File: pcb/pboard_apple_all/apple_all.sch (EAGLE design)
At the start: 33 parts, among them IC1 STM32F072C8T6, SW1 324_SW, SW2 324_SW

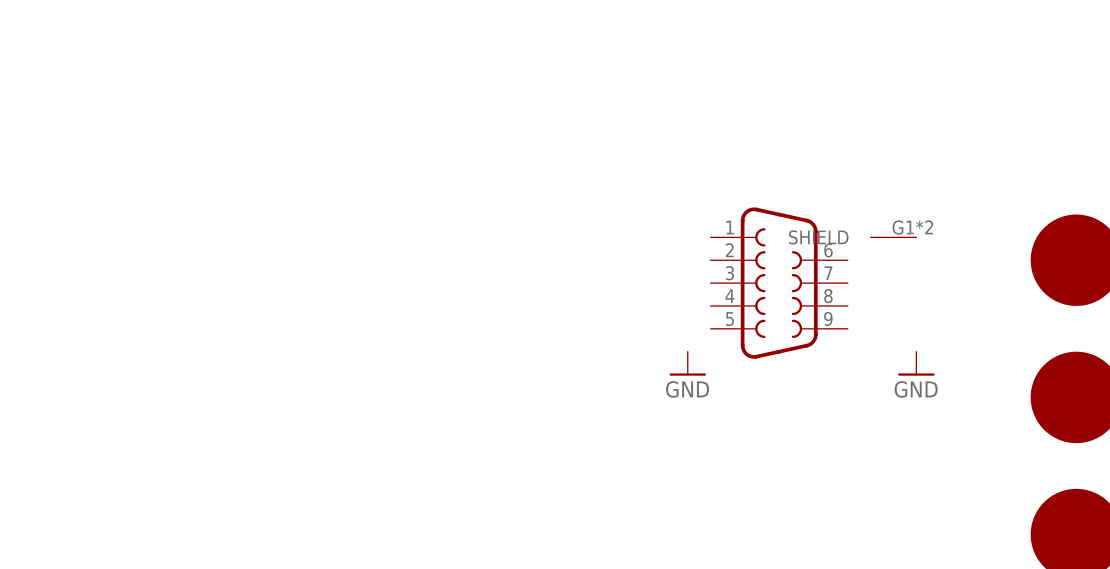
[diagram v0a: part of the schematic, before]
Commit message: started quad encoder test
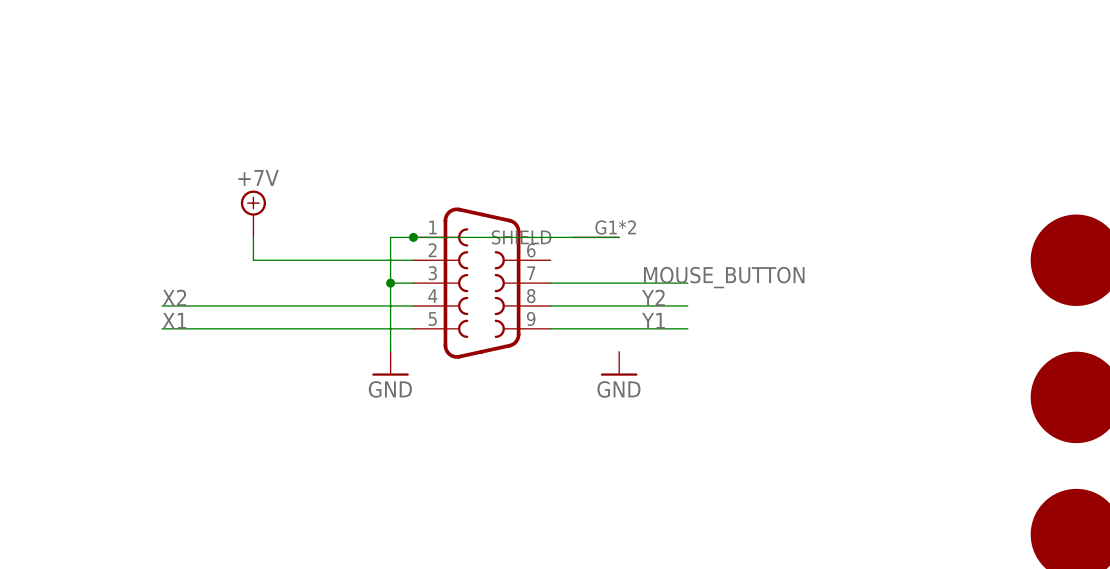
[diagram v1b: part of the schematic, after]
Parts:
- J2: device SparkFun-Connectors:DB9MALE -> SparkFun-Connectors:DB9FEMALE
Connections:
- new net +7V: J2.2
- new net MOUSE_BUTTON: J2.7
- new net X1: J2.5
- new net X2: J2.4
- new net Y1: J2.9
- new net Y2: J2.8
- net GND: now also J2.1, J2.3, J2.SHIELD
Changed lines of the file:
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@@
 <part name="U$7" library="f1c100s" deviceset="M2.5HOLE" device=""/>
 <part name="JP1" library="adafruit_changed" deviceset="PINHD-2X20" device="-BIG"/>
-<part name="J2" library="SparkFun-Connectors" deviceset="DB9" device="MALE"/>
+<part name="J2" library="SparkFun-Connectors" deviceset="DB9" device="FEMALE"/>
 <part name="SW1" library="3pos_slide_switch_centered" deviceset="324_SW" device="" value="324_SW"/>
 <part name="+3V1" library="supply1" library_urn="urn:adsk.eagle:library:371" deviceset="+3V3" device=""/>
@@
 <part name="U$5" library="adb" deviceset="ADB" device=""/>
 <part name="U$9" library="SparkFun-Retired" deviceset="RJ9" device="PTH"/>
+<part name="SUPPLY1" library="supply2" library_urn="urn:adsk.eagle:library:372" deviceset="+7V" device=""/>
 </parts>
 <sheets>
@@
 <attribute name="VALUE" x="85.09" y="-10.16" size="1.778" layer="96"/>
 </instance>
-<instance part="J2" gate="G$1" x="256.54" y="157.48" smashed="yes">
-<attribute name="VALUE" x="252.73" y="149.098" size="1.778" layer="96" font="vector" align="top-left"/>
+<instance part="J2" gate="G$1" x="223.52" y="157.48" smashed="yes">
+<attribute name="VALUE" x="219.71" y="149.098" size="1.778" layer="96" font="vector" align="top-left"/>
 </instance>
 <instance part="SW1" gate="G$1" x="-10.16" y="45.72" smashed="yes" rot="MR270"/>
@@
 <attribute name="VALUE" x="95.25" y="-47.498" size="1.778" layer="96" rot="MR180"/>
 </instance>
-<instance part="GND15" gate="1" x="246.38" y="147.32" smashed="yes">
-<attribute name="VALUE" x="243.84" y="144.78" size="1.778" layer="96"/>
-</instance>
-<instance part="GND16" gate="1" x="271.78" y="147.32" smashed="yes">
-<attribute name="VALUE" x="269.24" y="144.78" size="1.778" layer="96"/>
+<instance part="GND15" gate="1" x="213.36" y="147.32" smashed="yes">
+<attribute name="VALUE" x="210.82" y="144.78" size="1.778" layer="96"/>
+</instance>
+<instance part="GND16" gate="1" x="238.76" y="147.32" smashed="yes">
+<attribute name="VALUE" x="236.22" y="144.78" size="1.778" layer="96"/>
 </instance>
 <instance part="+3V10" gate="G$1" x="-30.48" y="63.5" smashed="yes" rot="MR0">
@@
 <attribute name="VALUE" x="-73.66" y="129.794" size="1.778" layer="96" font="vector"/>
 <attribute name="NAME" x="-73.66" y="145.288" size="1.778" layer="95" font="vector"/>
+</instance>
+<instance part="SUPPLY1" gate="G$1" x="198.12" y="165.1" smashed="yes">
+<attribute name="VALUE" x="196.215" y="168.275" size="1.778" layer="96"/>
 </instance>
 </instances>
@@
 <junction x="93.98" y="127"/>
 </segment>
+<segment>
+<pinref part="J2" gate="G$1" pin="1"/>
+<pinref part="GND15" gate="1" pin="GND"/>
+<wire x1="215.9" y1="162.56" x2="213.36" y2="162.56" width="0.1524" layer="91"/>
+<wire x1="213.36" y1="162.56" x2="213.36" y2="157.48" width="0.1524" layer="91"/>
+<pinref part="J2" gate="G$1" pin="3"/>
+<wire x1="213.36" y1="157.48" x2="213.36" y2="149.86" width="0.1524" layer="91"/>
+<wire x1="215.9" y1="157.48" x2="213.36" y2="157.48" width="0.1524" layer="91"/>
+<junction x="213.36" y="157.48"/>
+<pinref part="J2" gate="G$1" pin="SHIELD"/>
+<wire x1="215.9" y1="162.56" x2="238.76" y2="162.56" width="0.1524" layer="91"/>
+<junction x="215.9" y="162.56"/>
+</segment>
 </net>
 <net name="N$29" class="0">
@@
 </segment>
 </net>
+<net name="+7V" class="0">
+<segment>
+<pinref part="J2" gate="G$1" pin="2"/>
+<pinref part="SUPPLY1" gate="G$1" pin="+7V"/>
+<wire x1="215.9" y1="160.02" x2="198.12" y2="160.02" width="0.1524" layer="91"/>
+<wire x1="198.12" y1="160.02" x2="198.12" y2="162.56" width="0.1524" layer="91"/>
+</segment>
+</net>
+<net name="X2" class="0">
+<segment>
+<pinref part="J2" gate="G$1" pin="4"/>
+<wire x1="215.9" y1="154.94" x2="187.96" y2="154.94" width="0.1524" layer="91"/>
+<label x="187.96" y="154.94" size="1.778" layer="95"/>
+</segment>
+</net>
+<net name="X1" class="0">
+<segment>
+<pinref part="J2" gate="G$1" pin="5"/>
+<wire x1="215.9" y1="152.4" x2="187.96" y2="152.4" width="0.1524" layer="91"/>
+<label x="187.96" y="152.4" size="1.778" layer="95"/>
+</segment>
+</net>
+<net name="MOUSE_BUTTON" class="0">
+<segment>
+<pinref part="J2" gate="G$1" pin="7"/>
+<wire x1="231.14" y1="157.48" x2="246.38" y2="157.48" width="0.1524" layer="91"/>
+<label x="241.3" y="157.48" size="1.778" layer="95"/>
+</segment>
+</net>
+<net name="Y2" class="0">
+<segment>
+<pinref part="J2" gate="G$1" pin="8"/>
+<wire x1="246.38" y1="154.94" x2="231.14" y2="154.94" width="0.1524" layer="91"/>
+<label x="241.3" y="154.94" size="1.778" layer="95"/>
+</segment>
+</net>
+<net name="Y1" class="0">
+<segment>
+<pinref part="J2" gate="G$1" pin="9"/>
+<wire x1="246.38" y1="152.4" x2="231.14" y2="152.4" width="0.1524" layer="91"/>
+<label x="241.3" y="152.4" size="1.778" layer="95"/>
+</segment>
+</net>

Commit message: working on testing board
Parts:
- removed C6: 100nF, clock:CAP0805
- added JP4, JP5: (no value), pinhead:PINHD-2X4
- added JP6: (no value), pinhead:PINHD-2X5
- added JP7: (no value), pinhead:PINHD-1X5
- added JP8: (no value), pinhead:PINHD-1X2
- added JP9: (no value), pinhead:PINHD-1X4
- added R1, R10, R16, R17, R18, R19, R2, R20, R3, R4, R5, R6, R8: 5.1K, SparkFun-Passives:RESISTOR0805-RES
- added SW3: 324_SW, 3pos_slide_switch_centered:324_SW
- added U$11: RJ9PTH, SparkFun-Retired:RJ9PTH
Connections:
- removed net +7V: J2.2
- removed net MOUSE_BUTTON: J2.7
- removed net N$44: IC1PORTB_L.PB2
- removed net X1: J2.5
- removed net X2: J2.4
- removed net Y1: J2.9
- removed net Y2: J2.8
- new net KB_5V: IC1PORTB_L.PB2, JP4.7, JP4.8, JP5.1, JP5.2, JP9.4, R16.1, R17.1, R18.1, R19.1, R20.1, R6.1
- new net KB_CLK: IC1PORTB_L.PB0, JP4.3, JP4.4, JP5.5, JP5.6, JP9.2, R19.2, R20.2, U$11.3, U$9.2
- new net KB_DATA: IC1PORTB_L.PB1, JP4.5, JP4.6, JP5.3, JP5.4, JP9.3, R17.2, R18.2, U$11.2, U$9.3
- new net N$26: J2.1, JP6.1
- new net N$30: J2.2, JP6.3
- new net N$31: J2.3, JP6.5
- new net N$32: J2.4, JP6.7
- new net N$33: J2.5, JP6.9
- new net N$34: J2.6, JP6.2
- new net N$35: J2.7, JP6.4
- new net N$36: J2.8, JP6.6
- new net N$42: J2.9, JP6.8
- new net N$43: IC1PORTB_H.PB8, U$1.3, U$4.ADB_DATA, U$5.ADB_DATA, U$8.3
- new net N$46: IC1PORTB_L.PB5, SW3.2, SW3.3, U$1.2, U$4.PSW, U$5.PSW, U$8.2
- new net N$47: IC1PORTB_H.PB12, JP7.5, R1.2
- new net N$48: IC1PORTA_H.PA8, JP7.1, R5.2
- new net N$49: JP8.1, JP8.2, R1.1, R2.1, R3.1, R4.1, R5.1
- new net N$5: R8.2, U$11.4
- new net N$50: R6.2, U$11.1
- new net N$51: R16.2, U$9.4
- new net N$52: R10.2, U$9.1
- net +3V3: now also JP3.5; no longer JP3.6
- net +5V: no longer C6.2
- net GND: now also JP3.6, JP4.1, JP4.2, JP5.7, JP5.8, JP6.10, JP9.1, R10.1, R8.1, SW3.1, SW3.4; no longer C6.1, J2.1, J2.3, JP3.5
- net N$10: now also IC1PORTB_H.PB14, JP7.3, R3.2; no longer U$1.2, U$4.PSW, U$5.PSW, U$8.2
- net N$3: now also IC1PORTB_H.PB9
- net N$4: now also IC1PORTB_H.PB15, JP7.2, R4.2; no longer U$1.3, U$4.ADB_DATA, U$5.ADB_DATA, U$8.3
- net N$45: now also IC1PORTB_H.PB13, JP7.4, R2.2; no longer IC1PORTB_L.PB0, TP3.TP
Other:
- moved on the sheet: IC1PORTB_H, U$9

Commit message: forgot what i did
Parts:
- added TP1, TP2: TPTP12R, testpad:TPTP12R
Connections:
- new net N$11: IC1PORTB_L.PB4, TP3.TP
- new net N$17: IC1PORTB_H.PB10, TP1.TP
- new net N$19: IC1PORTB_H.PB11, TP2.TP
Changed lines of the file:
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@@
 <part name="GND14" library="supply1" deviceset="GND" device=""/>
 <part name="GND15" library="supply1" library_urn="urn:adsk.eagle:library:371" deviceset="GND" device=""/>
+<part name="TP1" library="testpad" library_urn="urn:adsk.eagle:library:385" deviceset="TP" device="TP12R" package3d_urn="urn:adsk.eagle:package:27963/1"/>
+<part name="TP2" library="testpad" library_urn="urn:adsk.eagle:library:385" deviceset="TP" device="TP12R" package3d_urn="urn:adsk.eagle:package:27963/1"/>
 </parts>
 <sheets>
@@
 <attribute name="VALUE" x="12.7" y="15.24" size="1.27" layer="96" font="vector" rot="MR0"/>
 </instance>
-<instance part="TP3" gate="G$1" x="25.4" y="60.96" smashed="yes">
-<attribute name="NAME" x="24.13" y="62.23" size="1.778" layer="95"/>
-<attribute name="TP_SIGNAL_NAME" x="26.67" y="59.69" size="1.778" layer="97"/>
+<instance part="TP3" gate="G$1" x="17.78" y="50.8" smashed="yes">
+<attribute name="TP_SIGNAL_NAME" x="19.05" y="49.53" size="1.778" layer="97"/>
 </instance>
 <instance part="P+2" gate="1" x="20.32" y="-38.1" smashed="yes" rot="MR0">
@@
 <instance part="GND15" gate="1" x="132.08" y="71.12" smashed="yes">
 <attribute name="VALUE" x="129.54" y="68.58" size="1.778" layer="96"/>
+</instance>
+<instance part="TP1" gate="G$1" x="60.96" y="180.34" smashed="yes">
+<attribute name="TP_SIGNAL_NAME" x="62.23" y="179.07" size="1.778" layer="97"/>
+</instance>
+<instance part="TP2" gate="G$1" x="55.88" y="177.8" smashed="yes">
+<attribute name="TP_SIGNAL_NAME" x="57.15" y="176.53" size="1.778" layer="97"/>
 </instance>
 </instances>
@@
 </segment>
 </net>
+<net name="N$11" class="0">
+<segment>
+<pinref part="IC1" gate="PORTB_L" pin="PB4"/>
+<pinref part="TP3" gate="G$1" pin="TP"/>
+<wire x1="43.18" y1="48.26" x2="17.78" y2="48.26" width="0.1524" layer="91"/>
+</segment>
+</net>
+<net name="N$17" class="0">
+<segment>
+<pinref part="IC1" gate="PORTB_H" pin="PB10"/>
+<pinref part="TP1" gate="G$1" pin="TP"/>
+<wire x1="86.36" y1="177.8" x2="60.96" y2="177.8" width="0.1524" layer="91"/>
+</segment>
+</net>
+<net name="N$19" class="0">
+<segment>
+<pinref part="IC1" gate="PORTB_H" pin="PB11"/>
+<pinref part="TP2" gate="G$1" pin="TP"/>
+<wire x1="86.36" y1="175.26" x2="55.88" y2="175.26" width="0.1524" layer="91"/>
+</segment>
+</net>
